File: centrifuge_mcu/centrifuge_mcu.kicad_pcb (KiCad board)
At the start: 6 copper layers, 114 parts, among them J101 Power Jumpers, J102 FPGA_Power, J103 FPGA_extra, J104 FPGA_control, J105 FPGA_SPI, J106 DDC_I2Cs, J107 ADC_I2C, J108 ADC_RST, J109 USB_B_Micro, J110 Barrel_Jack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

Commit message: do all MCU I think I can before merging in FPGA PCB
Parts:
- moved D101 9.04 mm to (114.5, 34.7)
- moved J113 6.35 mm to (182.2, 61.6)
- moved C149 3.37 mm to (125.3, 49.7), turned to -90 degrees
- moved C143 1.33 mm to (133.8, 49.8)
- moved C146 1.31 mm to (133.9, 52.1)
- moved C150 0.51 mm to (173.0, 81.3)
- moved C147 0.22 mm to (137.0, 58.0)
- moved C148 0.05 mm to (133.9, 47.5)
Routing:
- net /MCU/I2C1_SDA: track 2.29 -> 85.8 mm, vias 1 -> 2
- net /MCU/I2C1_SCL: track 1.89 -> 83.0 mm, vias 1 -> 2
- net /MCU/SPI1_MOSI: track 6.34 -> 84.0 mm, vias 0 -> 2
- net /MCU/SPI1_MISO: track 7.64 -> 68.4 mm
- net Net-(Q102-Pad1): track 0.56 -> 34.4 mm
- net (no net): track 1.56 -> 32.2 mm
- net Net-(J114-Pad6): track 0.78 -> 29.7 mm
- net Net-(J114-Pad4): track 0.63 -> 29.5 mm
- net +3.3V: track 194.0 -> 181.7 mm, vias 13 -> 16
- net /MCU/ADC1_RST: track 63.8 -> 60.9 mm
- net Net-(J114-Pad9): track 3.07 -> 0.18 mm
- net /Button Panel/C1: track 0.00 -> 2.85 mm
- net /Button Panel/R2: track 0.00 -> 2.65 mm
- net Net-(J113-Pad10): track 67.9 -> 65.3 mm
- net Net-(J114-Pad12): track 0.00 -> 2.54 mm
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
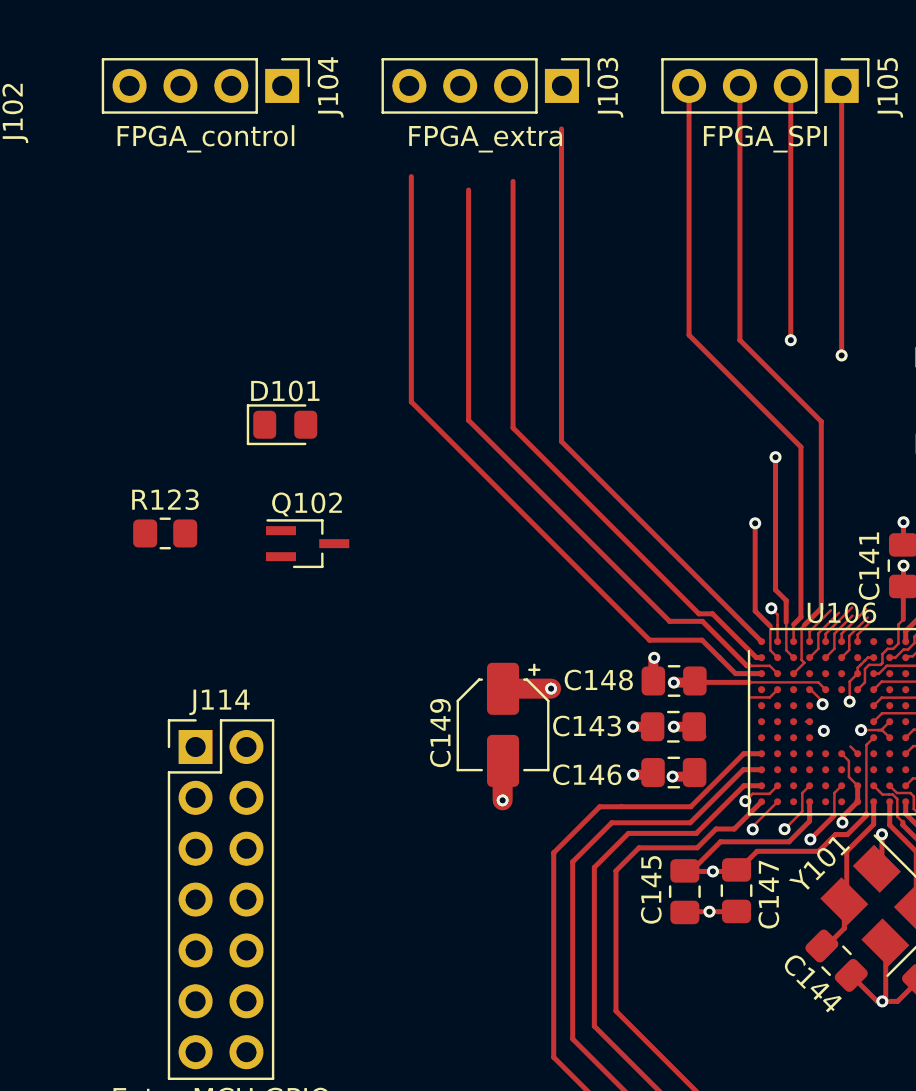
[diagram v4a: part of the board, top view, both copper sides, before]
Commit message: rebase with FPGA pcb, trying to add it
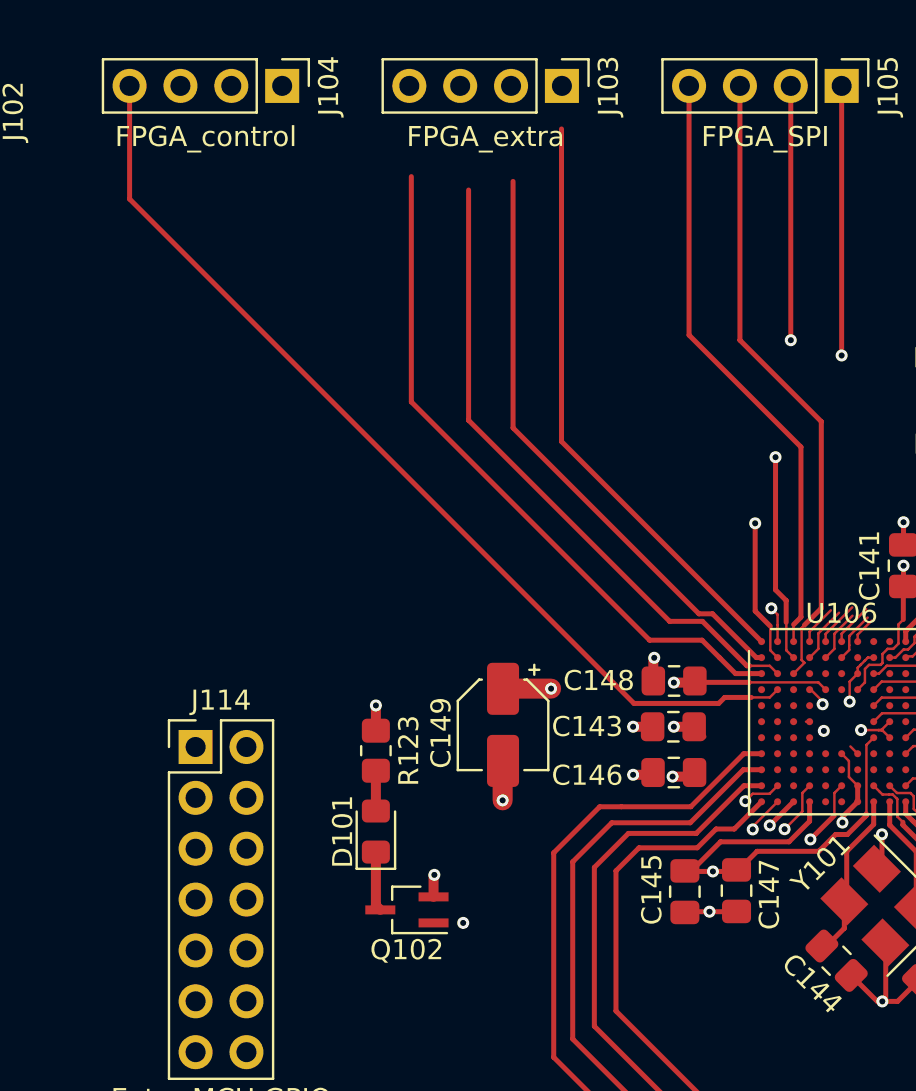
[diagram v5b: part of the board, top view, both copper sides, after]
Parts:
- moved D101 20.8 mm to (119.0, 55.0), turned to 90 degrees
- moved Q102 19.0 mm to (120.5, 58.9), turned to 180 degrees
- moved R123 15.1 mm to (119.0, 51.0), turned to -90 degrees
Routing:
- net /MCU/CMU_CLK#0: track 1.53 -> 48.8 mm
- net (no net): track 32.2 -> 51.3 mm, vias 0 -> 2
- net Net-(D101-Pad1): track 0.00 -> 2.98 mm
- net Net-(D101-Pad2): track 0.00 -> 2.01 mm
- net +3.3V: track 181.7 -> 182.9 mm, vias 16 -> 17
- net GND: track 117.9 -> 119.0 mm, vias 111 -> 112

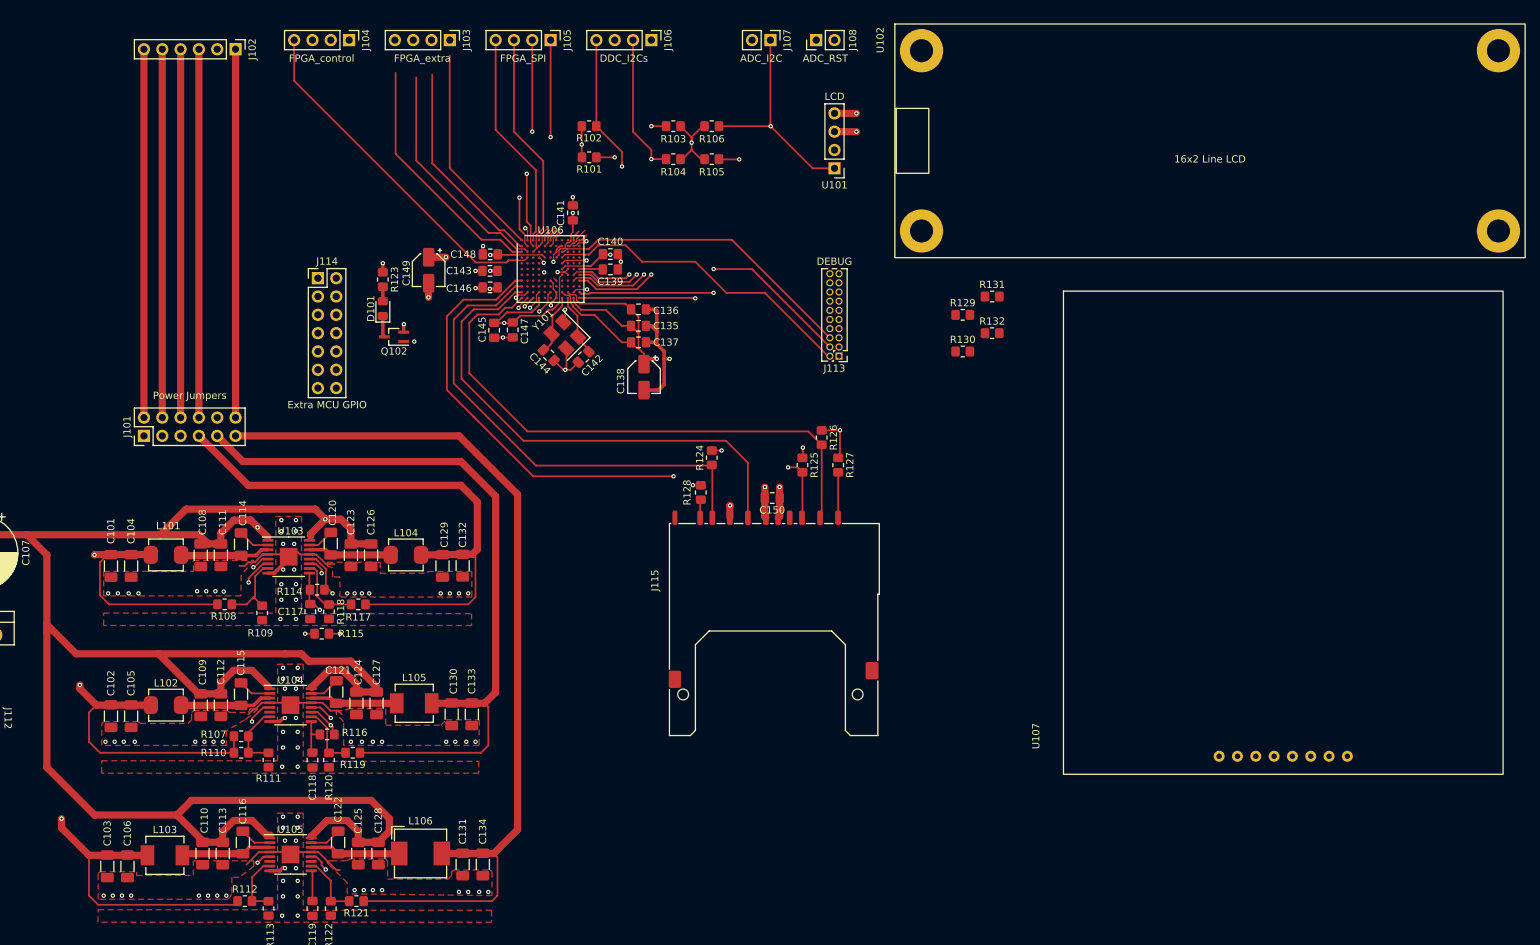
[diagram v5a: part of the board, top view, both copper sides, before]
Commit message: connect everything in MCU pcb, connection time
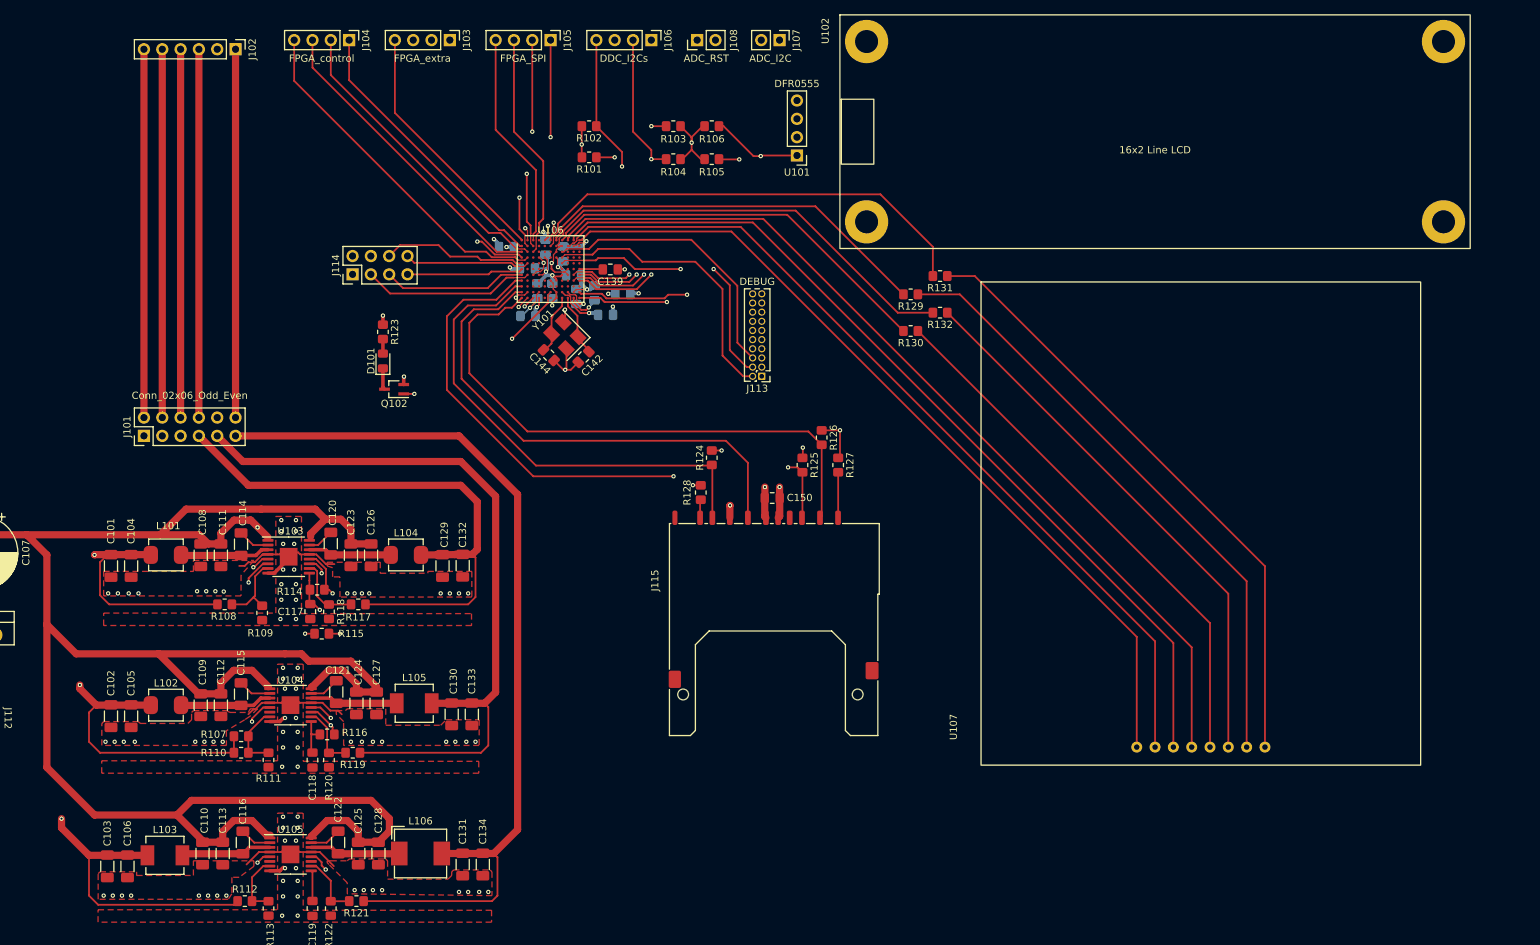
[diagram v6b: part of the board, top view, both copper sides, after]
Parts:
- C135, C136, C137, C140, C141, C143, C145, C146, C147, C148: moved to B.Cu
- C138, C149: footprint Capacitor_SMD:CP_Elec_4x5.4 -> Capacitor_SMD:C_0805_2012Metric_Pad1.18x1.45mm_HandSolder; moved to B.Cu
- J101: value Power Jumpers -> Conn_02x06_Odd_Even
- J114: footprint Connector_PinHeader_2.54mm:PinHeader_2x07_P2.54mm_Vertical -> Connector_PinHeader_2.54mm:PinHeader_2x04_P2.54mm_Vertical
- R114, R115, R116: value 100k -> 10k
- U101: value LCD -> DFR0555
- moved J108 16.5 mm to (162.6, 17.8)
- moved C148 11.9 mm to (145.4, 50.4), turned to 0 degrees
- moved C138 11.9 mm to (152.3, 53.0), turned to 0 degrees
- moved U107 11.5 mm to (232.4, 115.8)
- moved C149 11.3 mm to (136.1, 46.5), turned to 180 degrees
- moved J113 11.1 mm to (171.5, 64.4)
- moved C140 9.55 mm to (142.5, 52.6), turned to -90 degrees
- moved C136 8.82 mm to (145.8, 53.3), turned to 90 degrees
- moved C143 8.37 mm to (141.5, 46.5), turned to 90 degrees
- moved R129 7.76 mm to (192.2, 53.0), turned to 180 degrees
- moved R130 7.76 mm to (192.2, 58.1), turned to 180 degrees
- moved R131 7.76 mm to (196.2, 50.5), turned to 180 degrees
- moved R132 7.76 mm to (196.2, 55.6), turned to 180 degrees
- moved U102 7.73 mm to (226.1, 30.5)
- moved C135 7.62 mm to (148.3, 52.8), turned to 90 degrees
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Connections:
- J114 pad 2: Net-(J114-Pad2) -> GND
- J114 pad 3: GND -> Net-(J114-Pad3)
- U106 pad A1: Net-(J114-Pad6) -> /MCU/MF-IO3
- U106 pad A10: Net-(J114-Pad5) -> /Button Panel/C2
- U106 pad A11: Net-(J114-Pad2) -> /Button Panel/C0
- U106 pad A2: Net-(J114-Pad10) -> /MCU/MF-IO2
- U106 pad A4: /Button Panel/C0 -> (no net)
- U106 pad A5: /Button Panel/R3 -> /MCU/MF-IO1
- U106 pad A6: /MCU/FPGA_INIT_B -> /MCU/MF-IO0
- U106 pad A7: /MCU/FPGA_PROGRAM_B -> /Button Panel/R2
- U106 pad A8: /MCU/FPGA_CONFIG_DONE -> /Button Panel/R0
- U106 pad B1: Net-(J114-Pad4) -> /MCU/FPGA_CONFIG_DONE
- U106 pad B4: /Button Panel/C1 -> (no net)
- U106 pad B5: /Button Panel/R2 -> (no net)
- U106 pad B6: Net-(J114-Pad12) -> /Button Panel/R3
- U106 pad B7: (no net) -> /Button Panel/R1
- U106 pad B9: /Button Panel/C2 -> /Button Panel/C1
- U106 pad C1: Net-(Q102-Pad1) -> /MCU/FPGA_INIT_B
- U106 pad C10: Net-(J114-Pad14) -> (no net)
- U106 pad C2: (no net) -> /MCU/FPGA_PROGRAM_B
- U106 pad C4: /Button Panel/R0 -> (no net)
- U106 pad C5: /Button Panel/R1 -> (no net)
- U106 pad D1: (no net) -> Net-(J114-Pad4)
- U106 pad D6: Net-(J114-Pad8) -> (no net)
- U106 pad E1: (no net) -> Net-(J114-Pad6)
- U106 pad E2: (no net) -> Net-(J114-Pad8)
- U106 pad F1: (no net) -> Net-(J114-Pad7)
- U106 pad F3: Net-(J114-Pad11) -> (no net)
- U106 pad F4: Net-(J114-Pad9) -> (no net)
- U106 pad G1: Net-(J114-Pad13) -> Net-(J114-Pad5)
- U106 pad G2: Net-(J114-Pad7) -> Net-(J114-Pad3)
- U106 pad J10: /MCU/MF-IO2 -> (no net)
- U106 pad J11: /MCU/MF-IO3 -> (no net)
- U106 pad J8: /MCU/MF-IO0 -> (no net)
- U106 pad J9: /MCU/MF-IO1 -> (no net)
- U106 pad L3: (no net) -> Net-(Q102-Pad1)
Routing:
- net /Button Panel/C3: track 0.00 -> 126.5 mm
- net /Button Panel/C2: track 3.49 -> 123.1 mm
- net /Button Panel/C1: track 2.85 -> 121.2 mm
- net /Button Panel/C0: track 2.00 -> 116.4 mm
- net Net-(R131-Pad1): track 0.00 -> 85.8 mm
- net Net-(R129-Pad1): track 0.00 -> 85.1 mm
- net Net-(R132-Pad1): track 0.00 -> 76.4 mm
- net Net-(R130-Pad1): track 0.00 -> 74.5 mm
- net /Button Panel/R3: track 2.26 -> 64.3 mm
- net /Button Panel/R1: track 0.00 -> 60.8 mm
- net +3.3V: track 182.9 -> 123.0 mm
- net /Button Panel/R0: track 0.00 -> 55.7 mm
- net /Button Panel/R2: track 2.65 -> 55.8 mm
- net (no net): track 51.3 -> 0.00 mm, vias 2 -> 0
- net /MCU/FPGA_INIT_B: track 2.13 -> 43.4 mm
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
